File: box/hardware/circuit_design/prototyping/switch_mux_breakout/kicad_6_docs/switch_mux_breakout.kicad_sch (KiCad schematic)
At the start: 14 parts, among them J1 rpi_port, SW1 SW_DIP_x08, SW2 SW_DIP_x08, SW3 SW_DIP_x08, SW4 SW_DIP_x08, U1 MCP23S18T-E/SO, U2 MCP23S18T-E/SO

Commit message: Update switches to use I2C instead of SPI
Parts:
- removed J1: rpi_port, Connector_PinHeader_2.54mm:PinHeader_1x12_P2.54mm_Vertical, symbol Connector_Generic:Conn_01x12
- removed U1, U2: MCP23S18T-E/SO, Package_SO:SOIC-28W_7.5x17.9mm_P1.27mm, symbol custom_symbols:MCP23S18T-E/SO
- added J1: rpi_port, Connector_PinHeader_2.54mm:PinHeader_1x06_P2.54mm_Vertical, symbol Connector_Generic:Conn_01x06
- added JP2, JP3, JP4, JP5, JP6, JP7: SolderJumper_3_Open, Jumper:SolderJumper-3_P1.3mm_Open_Pad1.0x1.5mm, symbol Jumper:SolderJumper_3_Open
- added R2, R3, R4: 10k, Resistor_SMD:R_0805_2012Metric, symbol Device:R
- added U1, U2: PCA9555D, Package_SO:SOIC-24W_7.5x15.4mm_P1.27mm, symbol Interface_Expansion:PCA9555D
- renumbered R2 to R5
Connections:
- net +3V3: now also J1.1 (Pin_1), JP2.3 (B), JP3.3 (B), JP4.3 (B), JP5.3 (B), JP6.3 (B), JP7.3 (B), R2.1, R3.1, R4.1, U1.24 (VDD), U2.24 (VDD)
- net GND: now also J1.6 (Pin_6), JP2.1 (A), JP3.1 (A), JP4.1 (A), JP5.1 (A), JP6.1 (A), JP7.1 (A), U1.12 (VSS), U2.12 (VSS)
- net SW0: now also U1.4 (IO0_0)
- net SW1: now also U1.5 (IO0_1)
- net SW10: now also U1.15 (IO1_2)
- net SW11: now also U1.16 (IO1_3)
- net SW12: now also U1.17 (IO1_4)
- net SW13: now also U1.18 (IO1_5)
- net SW14: now also U1.19 (IO1_6)
- net SW15: now also U1.20 (IO1_7)
- net SW16: now also U2.4 (IO0_0)
- net SW17: now also U2.5 (IO0_1)
- net SW18: now also U2.6 (IO0_2)
- net SW19: now also U2.7 (IO0_3)
- net SW2: now also U1.6 (IO0_2)
- net SW20: now also U2.8 (IO0_4)
- net SW21: now also U2.9 (IO0_5)
- net SW22: now also U2.10 (IO0_6)
- net SW23: now also U2.11 (IO0_7)
- net SW24: now also U2.13 (IO1_0)
- net SW25: now also U2.14 (IO1_1)
- net SW26: now also U2.15 (IO1_2)
- net SW27: now also U2.16 (IO1_3)
- net SW28: now also U2.17 (IO1_4)
- net SW29: now also U2.18 (IO1_5)
- net SW3: now also U1.7 (IO0_3)
- net SW30: now also U2.19 (IO1_6)
- net SW31: now also U2.20 (IO1_7)
- net SW4: now also U1.8 (IO0_4)
- net SW5: now also U1.9 (IO0_5)
- net SW6: now also U1.10 (IO0_6)
- net SW7: now also U1.11 (IO0_7)
- net SW8: now also U1.13 (IO1_0)
- net SW9: now also U1.14 (IO1_1)
- net ~{RESET} renamed ~{INT 0-15}
- net ~{INT 0-15}: now also J1.4 (Pin_4), U1.1 (~{INT})
- new net A0 0-15: JP2.2 (C), U1.21 (A0)
- new net A0 16-31: JP5.2 (C), U2.21 (A0)
- new net A1 0-15: JP3.2 (C), U1.2 (A1)
- new net A1 16-31: JP6.2 (C), U2.2 (A1)
- new net A2 0-15: JP4.2 (C), U1.3 (A2)
- new net A2 16-31: JP7.2 (C), U2.3 (A2)
- new net SCL: J1.2 (Pin_2), R3.2, U1.22 (SCL), U2.22 (SCL)
- new net SDA: J1.3 (Pin_3), R4.2, U1.23 (SDA), U2.23 (SDA)
- new net ~{INT 16-31}: J1.5 (Pin_5), R2.2, U2.1 (~{INT})
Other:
- note added: "Address set for chip 1"
- note added: "Address set for chip 2"
- note added: "Simple breakout board for evaluating hardware. This board reads 32 switches via I2C. Each chip has an interrupt line which can be configured. The switches can be set to be active high or active low with a jumper."
- note removed: "Simple breakout board for evaluating hardware. This board reads 32 switches via SPI. Each chip has two interrupt lines which can be configured. The switches can be set to be active high or active low with a jumper."
- moved on the sheet: C1, C2, C3, D1, R5

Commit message: Make I2C address jumpers MSB first
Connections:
- net A0 0-15: now also JP4.2 (C); no longer JP2.2 (C)
- net A0 16-31: now also JP7.2 (C); no longer JP5.2 (C)
- net A2 0-15: now also JP2.2 (C); no longer JP4.2 (C)
- net A2 16-31: now also JP5.2 (C); no longer JP7.2 (C)
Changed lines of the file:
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@@
     (effects (font (size 1.27 1.27)) (justify left bottom))
   )
-  (label "A2 16-31" (at 85.09 149.86 180)
+  (label "A0 16-31" (at 85.09 149.86 180)
     (effects (font (size 1.27 1.27)) (justify right bottom))
   )
@@
     (effects (font (size 1.27 1.27)) (justify left bottom))
   )
-  (label "A2 0-15" (at 83.82 83.82 180)
+  (label "A0 0-15" (at 83.82 83.82 180)
     (effects (font (size 1.27 1.27)) (justify right bottom))
   )
@@
     (effects (font (size 1.27 1.27)) (justify left bottom))
   )
-  (label "A0 0-15" (at 46.99 83.82 180)
+  (label "A2 0-15" (at 46.99 83.82 180)
     (effects (font (size 1.27 1.27)) (justify right bottom))
   )
@@
     (effects (font (size 1.27 1.27)) (justify left bottom))
   )
-  (label "A0 16-31" (at 48.26 149.86 180)
+  (label "A2 16-31" (at 48.26 149.86 180)
     (effects (font (size 1.27 1.27)) (justify right bottom))
   )

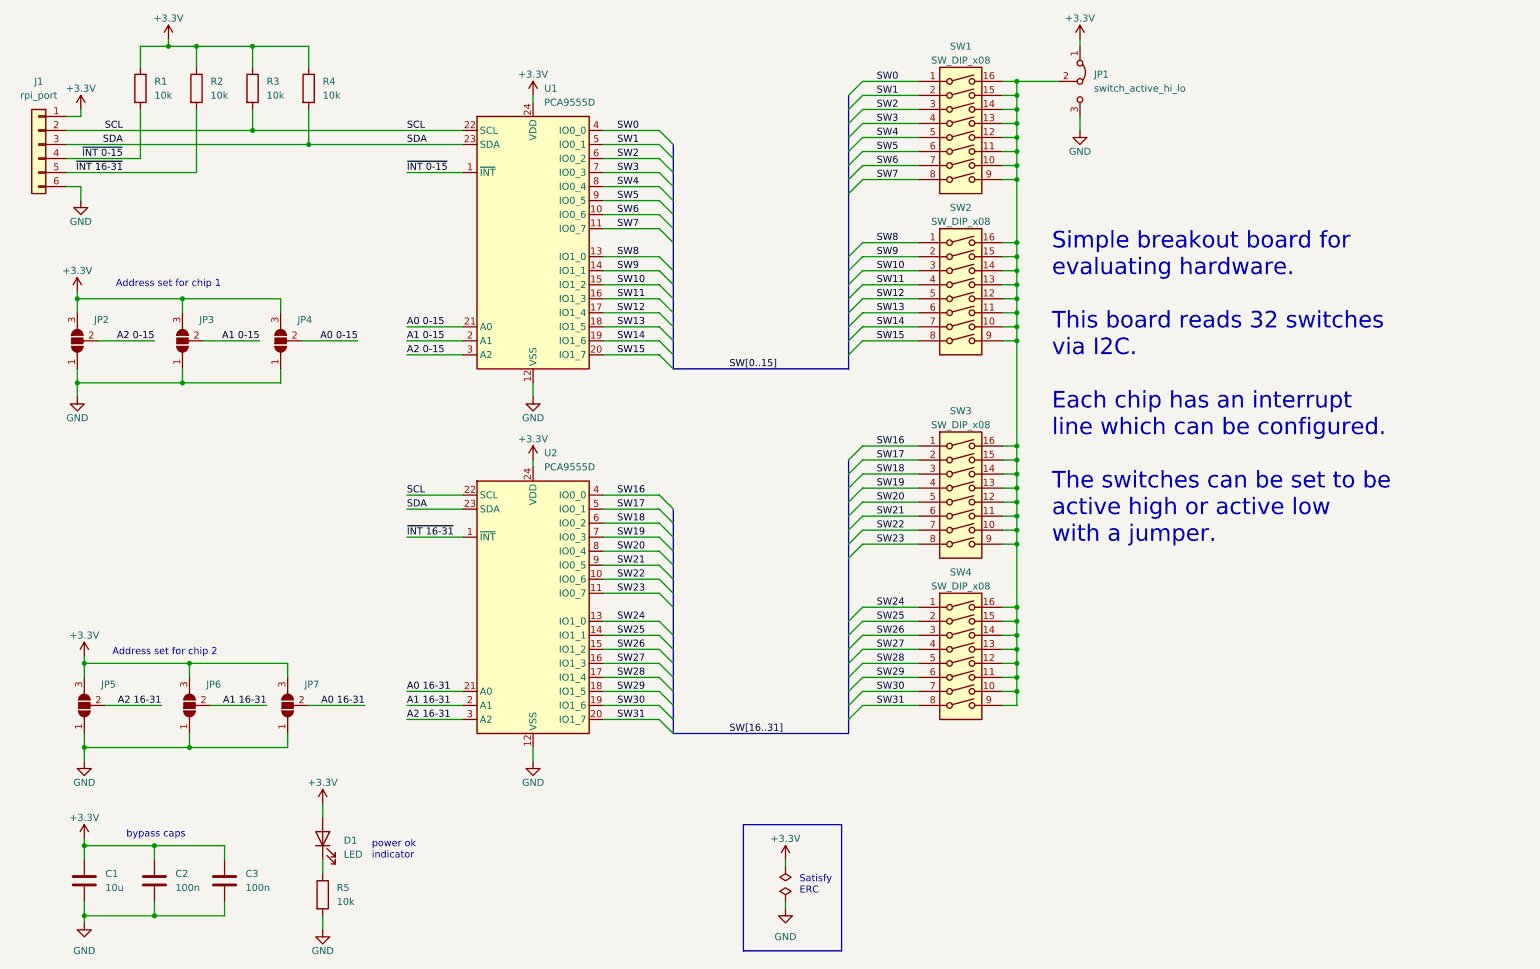
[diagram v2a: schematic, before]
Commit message: Change LED and switch breakouts, use headers instead of components
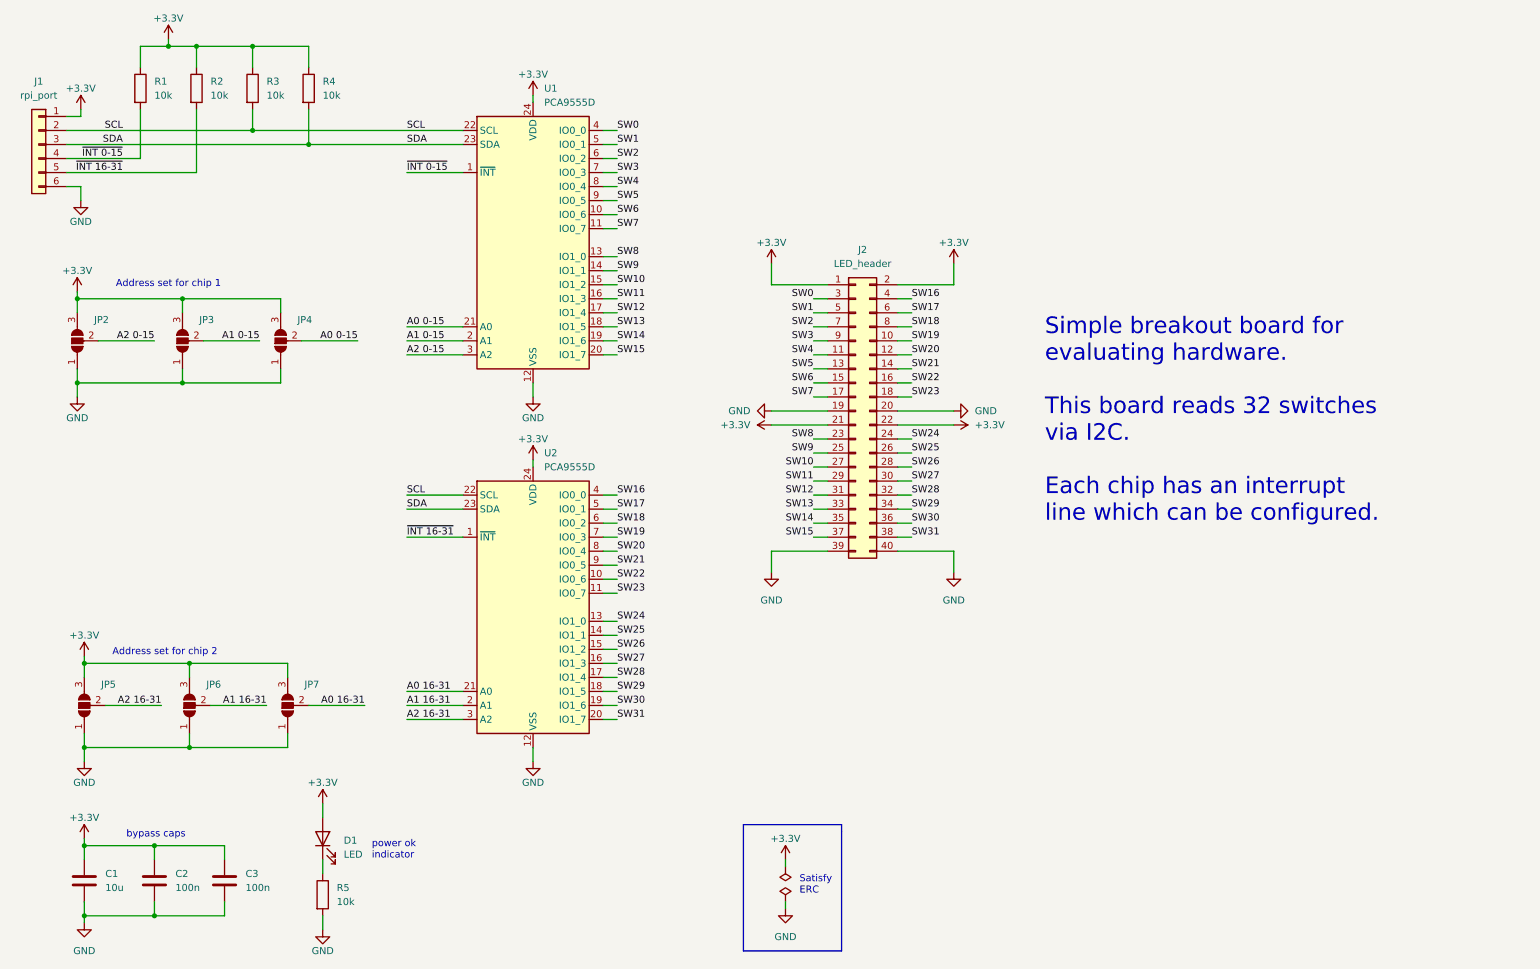
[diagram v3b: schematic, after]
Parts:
- removed JP1: switch_active_hi_lo, Connector_PinHeader_2.54mm:PinHeader_1x03_P2.54mm_Vertical, symbol Jumper:Jumper_3_Bridged12
- removed SW1, SW2, SW3, SW4: SW_DIP_x08, Button_Switch_THT:SW_DIP_SPSTx08_Slide_9.78x22.5mm_W7.62mm_P2.54mm, symbol Switch:SW_DIP_x08
- added J2: LED_header, Connector_PinHeader_2.54mm:PinHeader_2x20_P2.54mm_Vertical, symbol Connector_Generic:Conn_02x20_Odd_Even
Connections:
- net +3V3: now also J2.1 (Pin_1), J2.2 (Pin_2), J2.21 (Pin_21), J2.22 (Pin_22)
- net GND: now also J2.19 (Pin_19), J2.20 (Pin_20), J2.39 (Pin_39), J2.40 (Pin_40)
- net SW0: now also J2.3 (Pin_3)
- net SW1: now also J2.5 (Pin_5)
- net SW10: now also J2.27 (Pin_27)
- net SW11: now also J2.29 (Pin_29)
- net SW12: now also J2.31 (Pin_31)
- net SW13: now also J2.33 (Pin_33)
- net SW14: now also J2.35 (Pin_35)
- net SW15: now also J2.37 (Pin_37)
- net SW16: now also J2.4 (Pin_4)
- net SW17: now also J2.6 (Pin_6)
- net SW18: now also J2.8 (Pin_8)
- net SW19: now also J2.10 (Pin_10)
- net SW2: now also J2.7 (Pin_7)
- net SW20: now also J2.12 (Pin_12)
- net SW21: now also J2.14 (Pin_14)
- net SW22: now also J2.16 (Pin_16)
- net SW23: now also J2.18 (Pin_18)
- net SW24: now also J2.24 (Pin_24)
- net SW25: now also J2.26 (Pin_26)
- net SW26: now also J2.28 (Pin_28)
- net SW27: now also J2.30 (Pin_30)
- net SW28: now also J2.32 (Pin_32)
- net SW29: now also J2.34 (Pin_34)
- net SW3: now also J2.9 (Pin_9)
- net SW30: now also J2.36 (Pin_36)
- net SW31: now also J2.38 (Pin_38)
- net SW4: now also J2.11 (Pin_11)
- net SW5: now also J2.13 (Pin_13)
- net SW6: now also J2.15 (Pin_15)
- net SW7: now also J2.17 (Pin_17)
- net SW8: now also J2.23 (Pin_23)
- net SW9: now also J2.25 (Pin_25)
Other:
- note added: "Simple breakout board for evaluating hardware. This board reads 32 switches via I2C. Each chip has an interrupt line which can be configured."
- note removed: "Simple breakout board for evaluating hardware. This board reads 32 switches via I2C. Each chip has an interrupt line which can be configured. The switches can be set to be active high or active low with a jumper."
